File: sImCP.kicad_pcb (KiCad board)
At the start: 2 copper layers, 155.6 x 140 mm, 79 parts, among them J1 AVR-ISP-6, SW1 RESET, SW2 BOOT, U1 ATmega328P-AU, Y1 16MHz

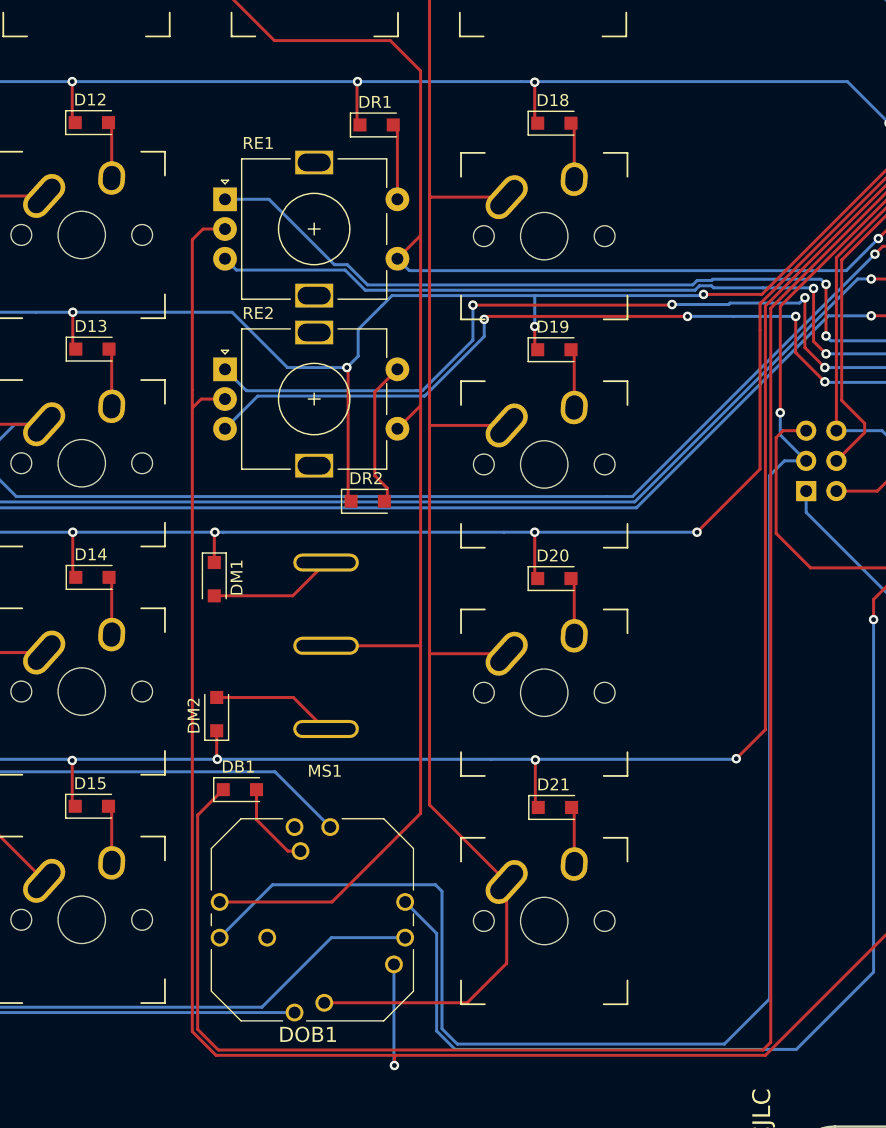
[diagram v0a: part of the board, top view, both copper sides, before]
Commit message: special parts spaced out
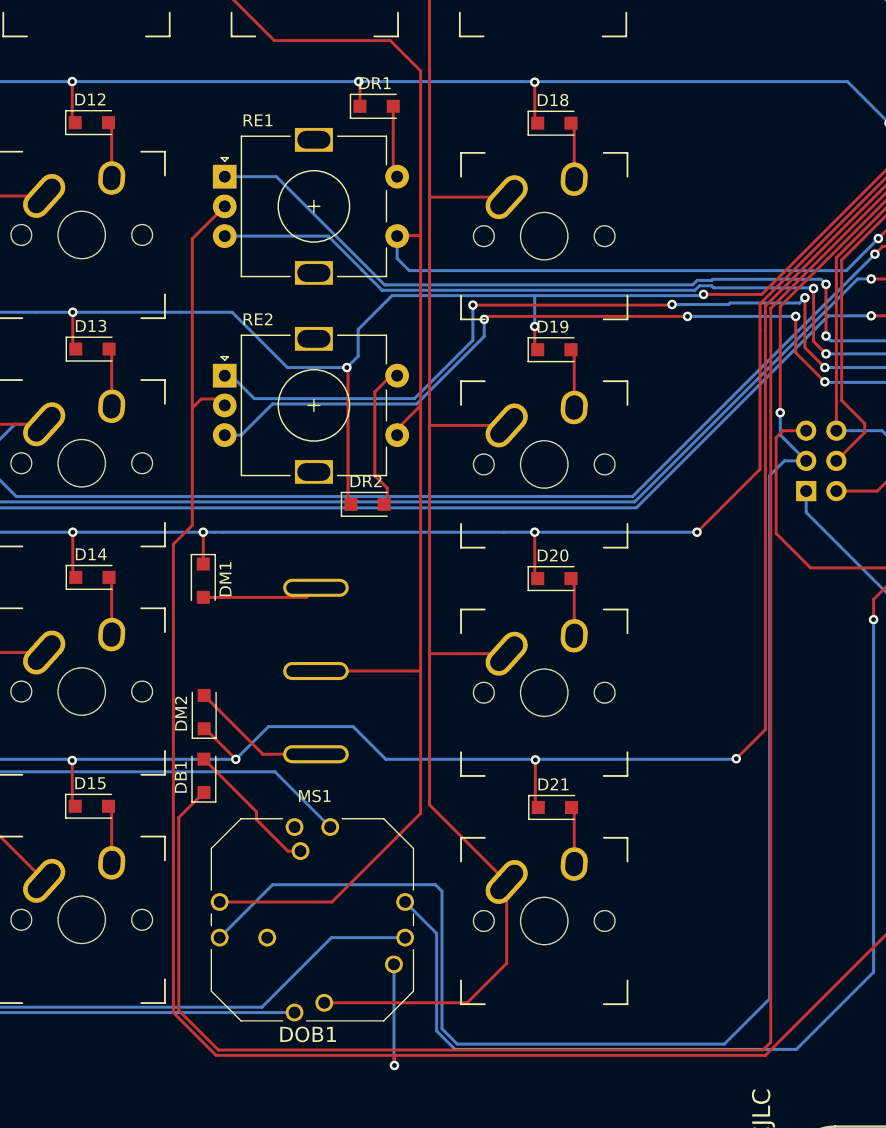
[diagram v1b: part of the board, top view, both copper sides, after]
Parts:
- moved DB1 3.24 mm to (161.9, 120.0), turned to 90 degrees
- moved MS1 2.29 mm to (171.3, 111.2)
- moved RE1 1.90 mm to (163.6, 69.6)
- moved DR1 1.57 mm to (176.4, 63.7)
- moved DM2 1.06 mm to (161.9, 114.6)
- moved DM1 0.94 mm to (161.8, 103.6)
- moved RE2 0.54 mm to (163.6, 86.3)
- moved DR2 0.26 mm to (175.6, 97.2)
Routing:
- net DOB1_COM: track 7.32 -> 11.7 mm
- net ROW4: track 190.2 -> 193.8 mm
- net GND: track 364.7 -> 366.9 mm
- net COL3: track 175.9 -> 177.9 mm
- net ROW1: track 150.7 -> 149.1 mm
- net MS1_2: track 10.3 -> 11.4 mm
- net R1B: track 69.6 -> 70.4 mm
- net R1A: track 70.4 -> 71.3 mm
- net MS1_1: track 10.6 -> 9.81 mm
- net R2A: track 75.1 -> 75.7 mm
